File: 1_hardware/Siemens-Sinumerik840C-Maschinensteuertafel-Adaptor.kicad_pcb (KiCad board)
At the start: 2 copper layers, 235 x 118.7 mm, 81 parts, among them J1 ProgHeader, J111 SSW-132-24-L-D, J121 SSW-132-24-L-D, J2 Power, J3 Buttons, J4 Reserve2, SW1 TS-1187A-B-A-B, SW2 TS-1187A-B-A-B, U1 STM32F103C8T6, U10 PCA9555PW,118, U11 PCA9555PW,118, U2 AP22652AW6-7, U3 LD1117S33CTR, U4 PCA9555PW,118, U5 PCA9555PW,118, U6 PCA9555PW,118, U7 PCA9555PW,118, U8 PCA9555PW,118, U9 PCA9555PW,118, X1 16MHz

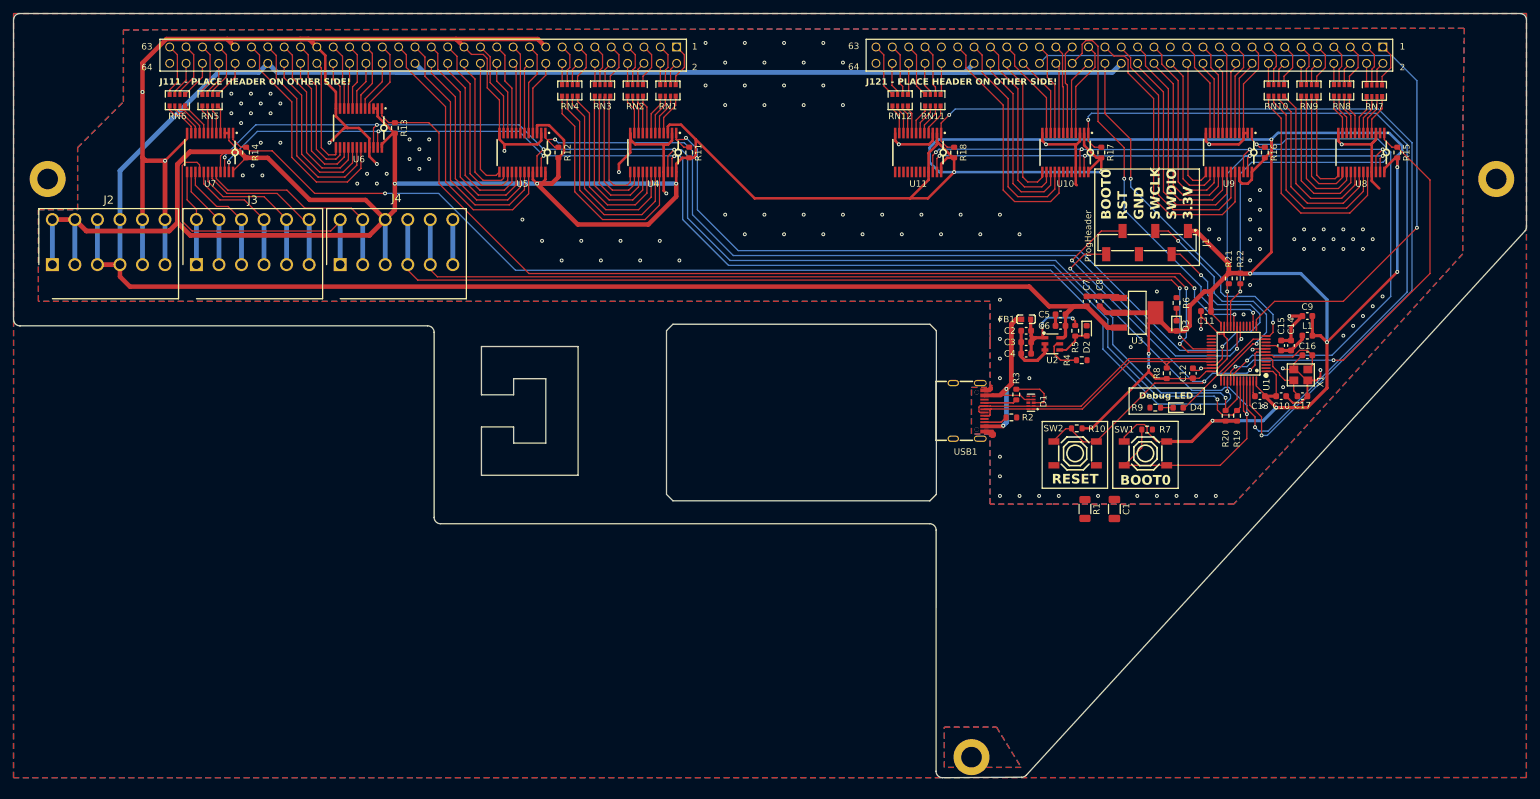
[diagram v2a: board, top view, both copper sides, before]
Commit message: changed from STM32F103C8 over to STM32L151C8 changed controller pinout, minor tweaks in board design, added labels and debug pads
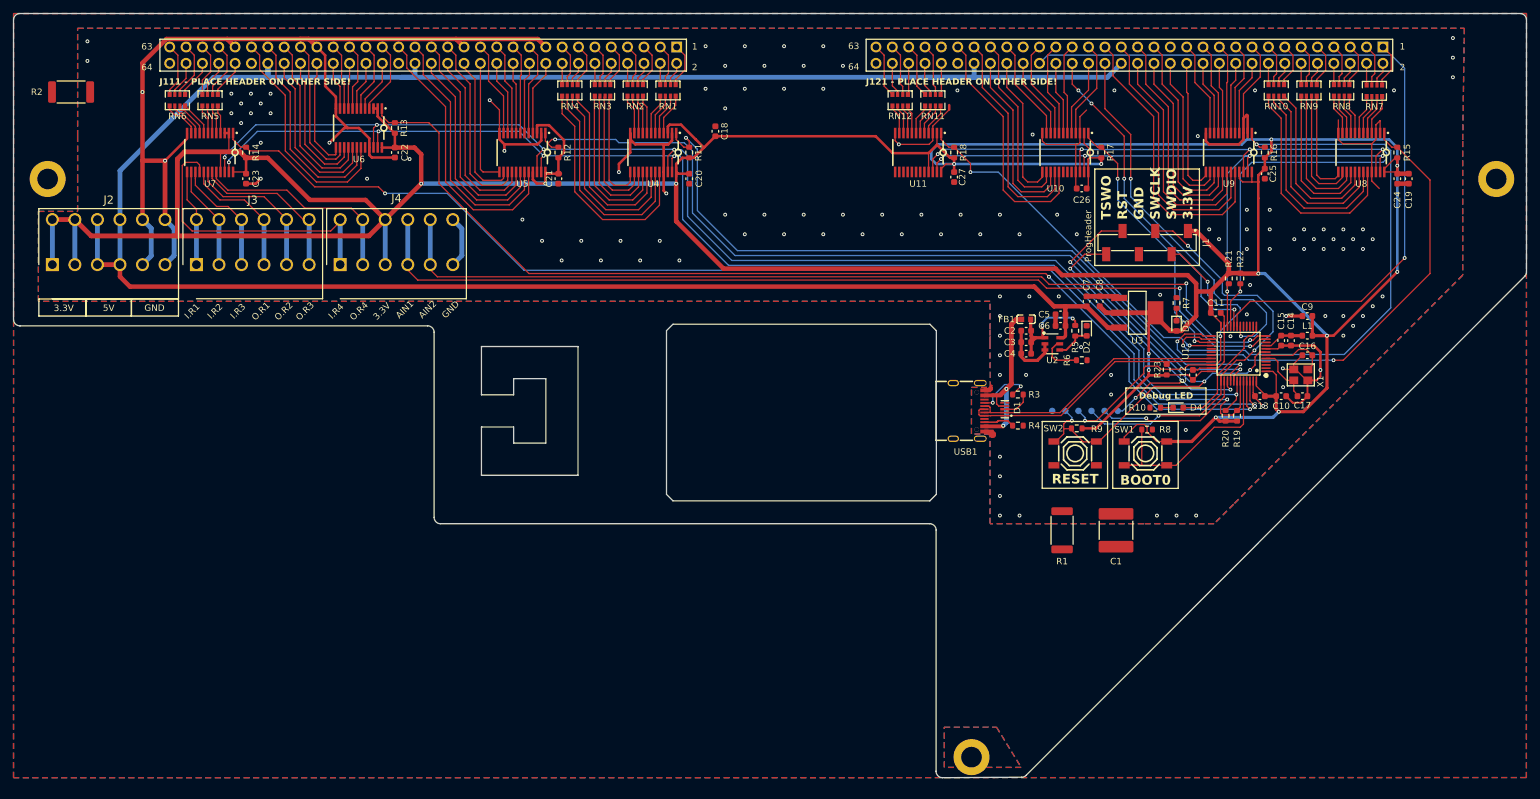
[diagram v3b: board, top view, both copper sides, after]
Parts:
- removed the R8 at (216.7, 81.4)
- added C18: 4u7, Capacitor_SMD:C_0603_1608Metric, F.Cu at (146.6, 43.8)
- added C19: 4u7, Capacitor_SMD:C_0603_1608Metric, F.Cu at (254.3, 51.1)
- added C20: 100n, Capacitor_SMD:C_0603_1608Metric, F.Cu at (142.5, 51.1)
- added C21: 100n, Capacitor_SMD:C_0603_1608Metric, F.Cu at (122.2, 51.1)
- added C22: 100n, Capacitor_SMD:C_0603_1608Metric, F.Cu at (96.8, 47.1)
- added C23: 100n, Capacitor_SMD:C_0603_1608Metric, F.Cu at (73.7, 51.1)
- added C24: 100n, Capacitor_SMD:C_0603_1608Metric, F.Cu at (252.5, 51.1)
- added C25: 100n, Capacitor_SMD:C_0603_1608Metric, F.Cu at (232.0, 50.4)
- added C26: 100n, Capacitor_SMD:C_0603_1608Metric, F.Cu at (203.5, 52.7)
- added C27: 100n, Capacitor_SMD:C_0603_1608Metric, F.Cu at (183.7, 50.9)
- added R2: 100k, Resistor_SMD:R_2512_6332Metric, F.Cu at (46.5, 37.7)
- added R23: 1k5, Resistor_SMD:R_0603_1608Metric, F.Cu at (216.7, 80.8)
- added TP1: JTDO-TraceSWO, TestPoint:TestPoint_Pad_D1.0mm, B.Cu at (209.1, 87.2)
- added TP2: JTDI, TestPoint:TestPoint_Pad_D1.0mm, B.Cu at (207.1, 87.2)
- added TP3: JTCK-SWCLK, TestPoint:TestPoint_Pad_D1.0mm, B.Cu at (205.0, 87.2)
- added TP4: JTMS-SWDIO, TestPoint:TestPoint_Pad_D1.0mm, B.Cu at (203.0, 87.2)
- added TP5: RESET, TestPoint:TestPoint_Pad_D1.0mm, B.Cu at (201.0, 87.2)
- added TP6: GND, TestPoint:TestPoint_Pad_D1.0mm, B.Cu at (198.9, 87.2)
- C1: footprint Capacitor_SMD:C_1206_3216Metric -> Capacitor_SMD:C_2220_5750Metric
- R1: footprint Resistor_SMD:R_1206_3216Metric -> Resistor_SMD:R_2512_6332Metric
- R10: renamed from R9; value 1k5 -> 470
- R5: value 10k -> 680
- R7: renamed from R6; value 1k5 -> 470
- RN1, RN10, RN11, RN12, RN2, RN3, RN4, RN5, RN6, RN7, RN8, RN9: value 4x680R -> 4x470R
- U1: value STM32F103C8T6 -> STM32L151C8T6
- moved R1 4.85 mm to (200.5, 105.8)
- moved D1 4.19 mm to (191.6, 87.0)
- moved C1 3.31 mm to (208.8, 105.8)
- moved R4 1.63 mm to (193.6, 89.5)
- moved C11 1.55 mm to (224.3, 72.0), turned to 180 degrees
- moved C14 0.76 mm to (236.0, 76.3), turned to 90 degrees
- moved C15 0.76 mm to (234.5, 76.3), turned to 90 degrees
- moved R3 0.25 mm to (193.6, 84.7), turned to 180 degrees
- moved C12 0.25 mm to (220.8, 81.6)
- renumbered R2 to R4, R4 to R6, R7 to R8, R10 to R9
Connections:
- J1 pad 6: BOOT0 -> TSWO
- U1 pad 11: DebugLED -> AIN1
- U1 pad 12: Button-~{A15} -> AIN2
- U1 pad 13: Button-~{D01} -> DebugLED
- U1 pad 14: Button-~{E01} -> unconnected-(U1-PA4-Pad14)
- U1 pad 18: EXP_INT1 -> Button-~{A15}
- U1 pad 19: EXP_INT2 -> Button-~{D01}
- U1 pad 20: EXP_INT3 -> Button-~{E01}
- U1 pad 25: unconnected-(U1-PB12-Pad25) -> EXP_INT5
- U1 pad 26: unconnected-(U1-PB13-Pad26) -> EXP_INT6
- U1 pad 27: unconnected-(U1-PB14-Pad27) -> EXP_INT7
- U1 pad 28: unconnected-(U1-PB15-Pad28) -> EXP_INT8
- U1 pad 29: AIN1 -> unconnected-(U1-PA8-Pad29)
- U1 pad 30: AIN2 -> unconnected-(U1-PA9-Pad30)
- U1 pad 38: unconnected-(U1-PA15-Pad38) -> /JTDI
- U1 pad 39: EXP_INT4 -> TSWO
- U1 pad 40: EXP_INT5 -> EXP_INT1
- U1 pad 41: EXP_INT6 -> EXP_INT2
- U1 pad 45: EXP_INT7 -> EXP_INT3
- U1 pad 46: EXP_INT8 -> EXP_INT4
- U10 pad 7: ENC1-X15 -> Button-E02
- U10 pad 8: Button-E02 -> ENC1-X15
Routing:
- net EXP_INT8: track 146.3 -> 57.2 mm
- net EXP_INT7: track 121.5 -> 42.2 mm
- net TSWO: track 0.00 -> 52.7 mm, vias 0 -> 4
- net +3V3: track 695.4 -> 741.1 mm
- net BOOT0: track 81.1 -> 36.2 mm, vias 2 -> 0
- net SWCLK: track 37.7 -> 64.5 mm, vias 2 -> 3
- net /JTDI: track 0.00 -> 23.2 mm, vias 0 -> 1
- net SWDIO: track 31.5 -> 52.5 mm, vias 2 -> 3
- net GND: track 373.0 -> 388.8 mm, vias 136 -> 129
- net EXP_INT5: track 64.0 -> 77.9 mm
- net EXP_INT3: track 153.7 -> 166.3 mm
- net EXP_INT6: track 78.5 -> 90.5 mm
- net Button-~{E01}: track 63.4 -> 53.2 mm, vias 2 -> 4
- net AIN1: track 142.2 -> 148.6 mm
- net AIN2: track 140.9 -> 145.8 mm
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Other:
- outline, holes or cut-outs redrawn
- board text added: "5V"
- board text added: "AIN1"
- board text added: "AIN2"
- board text added: "I.R1"
- board text added: "I.R2"
- board text added: "I.R3"
- board text added: "I.R4"
- board text added: "JTDI"
- board text added: "O.R1"
- board text added: "O.R2"
- board text added: "O.R3"
- board text added: "O.R4"
- board text added: "TSWO"
- board text added: "TraceSWO"

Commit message: finished v0.9.2
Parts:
- added G***: LOGO, LOGO, F.Cu at (168.5, 40.2)
- added R24: 0, Resistor_SMD:R_0603_1608Metric, F.Cu at (181.7, 55.7)
- added R25: 0, Resistor_SMD:R_0603_1608Metric, F.Cu at (179.9, 55.7)
- added R26: 0, Resistor_SMD:R_0603_1608Metric, F.Cu at (227.9, 65.4)
- added R27: 0, Resistor_SMD:R_0603_1608Metric, F.Cu at (226.1, 65.4)
- C12: renamed from C15; value 100n -> 1u
- C13: renamed from C14; value 1u -> 100n
- C19: value 4u7 -> 100n
- C23: value 100n -> 4u7
- RN1, RN10, RN11, RN12, RN2, RN3, RN4, RN5, RN6, RN7, RN8, RN9: value 4x470R -> 4x680R
- TP1: value JTDO-TraceSWO -> GND
- TP3: value JTCK-SWCLK -> JTMS-SWDIO
- TP4: value JTMS-SWDIO -> JTCK-SWCLK
- TP5: value RESET -> JTDO-TraceSWO
- TP6: value GND -> RESET
- moved R12 22.6 mm to (207.3, 78.1)
- moved R13 19.5 mm to (209.1, 78.1)
- moved R22 5.34 mm to (226.1, 61.3)
- moved R23 5.34 mm to (227.9, 61.3)
- moved C18 2.65 mm to (145.8, 41.2), turned to 180 degrees
- moved R8 0.06 mm to (216.7, 80.9)
- renumbered C12 to C14, C13 to C15, R9 to R11, R19 to R12, R20 to R13, R11 to R14, R12 to R15, R13 to R16, R14 to R17, R15 to R18, R16 to R19, R17 to R20, R18 to R21, R21 to R22, R22 to R23, R23 to R8, R8 to R9
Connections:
- net /JTDI renamed /Microcontroller/JTDI
- C18 pad 2: +3V3 -> VCC
- C19 pad 2: +3V3 -> VCC
- C20 pad 2: +3V3 -> VCC
- C21 pad 2: +3V3 -> VCC
- C22 pad 2: +3V3 -> VCC
- C23 pad 2: +3V3 -> VCC
- C24 pad 2: +3V3 -> VCC
- C25 pad 2: +3V3 -> VCC
- C26 pad 2: +3V3 -> VCC
- C27 pad 2: +3V3 -> VCC
- R12 pad 2: +3V3 -> VCC
- R13 pad 2: +3V3 -> VCC
- R14 pad 2: +3V3 -> VCC
- R15 pad 2: +3V3 -> VCC
- R16 pad 2: +3V3 -> VCC
- R17 pad 2: +3V3 -> VCC
- R18 pad 2: +3V3 -> VCC
- R19 pad 2: +3V3 -> VCC
- R20 pad 2: +3V3 -> VCC
- R21 pad 2: +3V3 -> VCC
- R22 pad 2: +3V3 -> VCC
- R23 pad 2: +3V3 -> VCC
- TP1 pad 1: TSWO -> GND
- TP3 pad 1: SWCLK -> SWDIO
- TP4 pad 1: SWDIO -> SWCLK
- TP5 pad 1: RST -> TSWO
- TP6 pad 1: GND -> RST
- U1 pad 18: Button-~{A15} -> unconnected-(U1-PB0-Pad18)
- U1 pad 19: Button-~{D01} -> unconnected-(U1-PB1-Pad19)
- U1 pad 20: Button-~{E01} -> unconnected-(U1-PB2-Pad20)
- U1 pad 21: I2C2_SCL -> Net-(U1-PB10)
- U1 pad 22: I2C2_SDA -> Net-(U1-PB11)
- U10 pad 10: Button-D02 -> Button-E02
- U10 pad 11: ENC1-X14 -> ENC1-X13
- U10 pad 13: Schluessel2 -> Button-~{D01}
- U10 pad 14: Button-A14 -> Button-D02
- U10 pad 15: Schluessel0 -> ENC1-X14
- U10 pad 16: Schluessel3 -> Schluessel2
- U10 pad 17: Button-A13 -> Button-A14
- U10 pad 18: unconnected-(U10-IO1_5-Pad18) -> Schluessel0
- U10 pad 19: unconnected-(U10-IO1_6-Pad19) -> Schluessel3
- U10 pad 2: +3V3 -> VCC
- U10 pad 20: unconnected-(U10-IO1_7-Pad20) -> Button-A13
- U10 pad 24: +3V3 -> VCC
- U10 pad 4: ENC1-X11 -> Button-~{A15}
- U10 pad 5: Button-A16 -> ENC1-X11
- U10 pad 6: ENC1-X12 -> Button-A16
- U10 pad 7: Button-E02 -> ENC1-X12
- U10 pad 8: ENC1-X15 -> Button-~{E01}
- U10 pad 9: ENC1-X13 -> ENC1-X15
- U11 pad 2: +3V3 -> VCC
- U11 pad 21: +3V3 -> VCC
- U11 pad 24: +3V3 -> VCC
- U4 pad 24: +3V3 -> VCC
- U4 pad 3: +3V3 -> VCC
- U5 pad 21: +3V3 -> VCC
- U5 pad 24: +3V3 -> VCC
- U5 pad 3: +3V3 -> VCC
- U6 pad 2: +3V3 -> VCC
- U6 pad 24: +3V3 -> VCC
- U6 pad 3: +3V3 -> VCC
- U7 pad 2: +3V3 -> VCC
- U7 pad 21: +3V3 -> VCC
- U7 pad 24: +3V3 -> VCC
- U7 pad 3: +3V3 -> VCC
- U8 pad 24: +3V3 -> VCC
- U9 pad 21: +3V3 -> VCC
- U9 pad 24: +3V3 -> VCC
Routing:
- net +3V3: track 741.1 -> 361.6 mm, vias 14 -> 5
- net VCC: track 372.8 -> 675.2 mm, vias 0 -> 5
- net Button-~{D01}: track 119.1 -> 23.3 mm, vias 1 -> 0
- net GND: track 388.8 -> 302.6 mm, vias 129 -> 113
- net Button-~{A15}: track 60.2 -> 12.7 mm, vias 2 -> 0
- net Button-~{E01}: track 53.2 -> 11.7 mm, vias 4 -> 0
- net ENC1-X14: track 15.9 -> 30.2 mm
- net Button-D02: track 12.6 -> 25.0 mm
- net Net-(U1-PB10): track 0.00 -> 8.40 mm
- net TSWO: track 52.7 -> 60.8 mm
- net Net-(U1-PB11): track 0.00 -> 7.89 mm
- net Schluessel2: track 23.2 -> 29.4 mm
- net Button-A14: track 29.2 -> 35.1 mm
- net Schluessel0: track 29.0 -> 34.7 mm
- net Schluessel3: track 35.0 -> 40.3 mm
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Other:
- board text added: "${ISSUE_DATE} ©PedPEx ${REVISION}"

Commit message: pcb v0.9.3 finished
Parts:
- removed the C5 at (200.2, 72.2)
- added C6: 100u, Capacitor_SMD:CP_Elec_5x5.8, F.Cu at (199.4, 69.9)
- C5: renamed from C6; value 120u -> 0.1u
- moved C7 0.51 mm to (204.8, 70.2)
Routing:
- net GND: track 302.6 -> 330.3 mm, vias 113 -> 116
- net +3V3: track 361.6 -> 363.9 mm
- net VCC: track 675.2 -> 676.2 mm

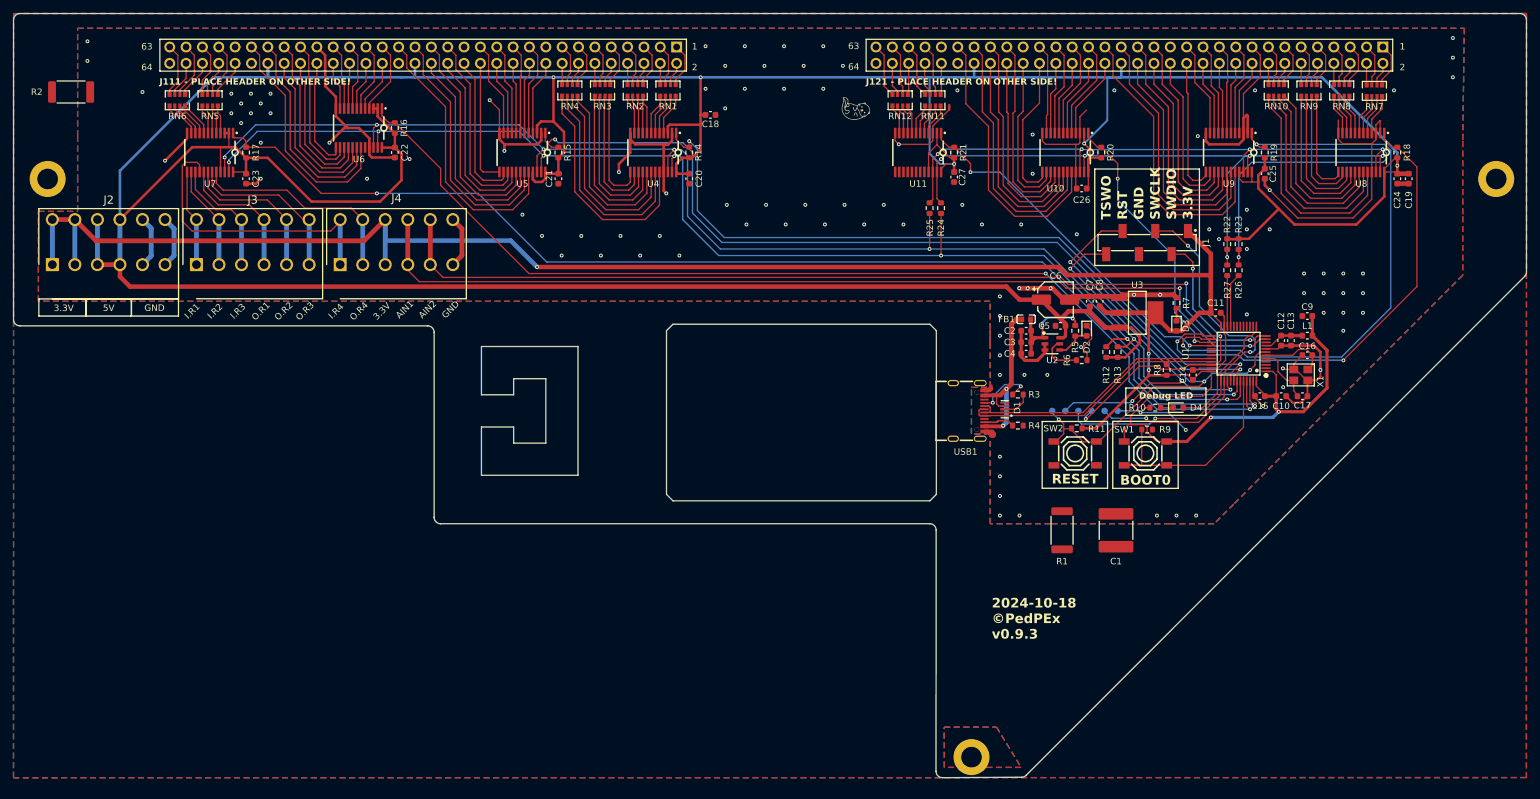
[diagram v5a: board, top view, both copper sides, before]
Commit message: PCB v0.9.4 - finished final prototype STM32 project reinitialised (F103C8 -> L151C8)
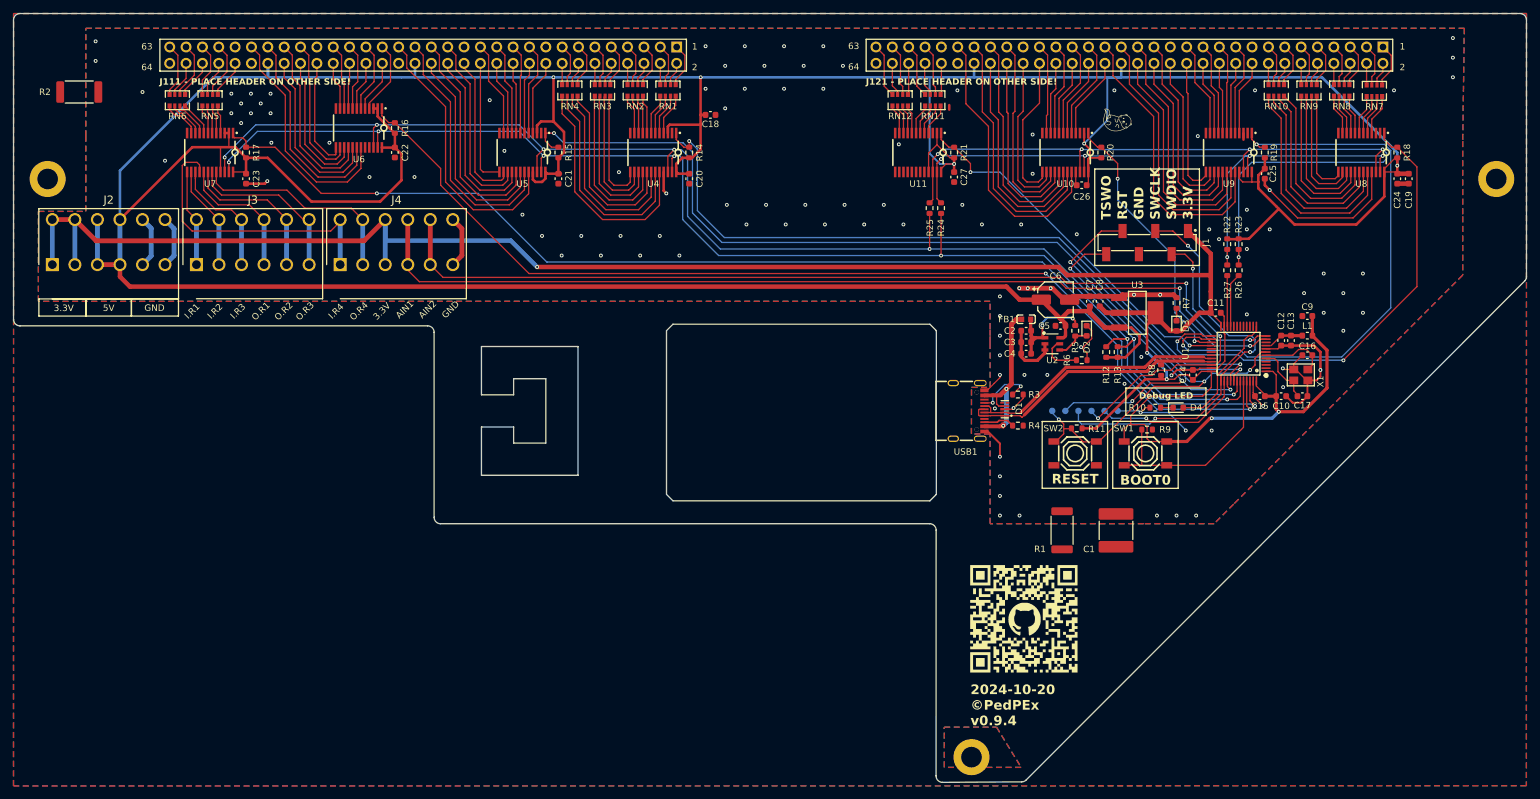
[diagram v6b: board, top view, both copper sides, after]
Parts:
- added G***: LOGO, project_library:QR_CODE, F.Cu at (194.5, 119.5)
- D1: footprint easyeda2kicad:USON-10_L2.5-W1.0-P0.50-BL -> project_library:USON-10_L2.5-W1.0-P0.50-BL
- G***: footprint LOGO -> project_library:LOGO
- H1, H2, H3: footprint MountingHole:MountingHole_3.2mm_M3_DIN965_Pad -> project_library:MountingHole_3.2mm_M3_DIN965_Pad
- J1: footprint easyeda2kicad:HDR-SMD_6P-P2.54-V-M-LS4.8_R2 -> project_library:HDR-SMD_6P-P2.54-V-M-LS4.8_R2
- J111, J121: footprint CostumLibrary:SAMTEC_SSW-132-24-L-D -> project_library:SAMTEC_SSW-132-24-L-D
- J2, J3, J4: footprint CostumLibrary:1824460000 - LSF-SMT 3.500690 3.5SN BK TU -> project_library:1824460000 - LSF-SMT 3.500690 3.5SN BK TU
- RN1, RN10, RN11, RN12, RN2, RN3, RN4, RN5, RN6, RN7, RN8, RN9: footprint easyeda2kicad:RES-ARRAY-SMD_0603-8P-L3.2-W1.6-BL -> project_library:RES-ARRAY-SMD_0603-8P-L3.2-W1.6-BL
- SW1, SW2: footprint easyeda2kicad:SW-SMD_4P-L5.1-W5.1-P3.70-LS6.5-TL-2 -> project_library:SW-SMD_4P-L5.1-W5.1-P3.70-LS6.5-TL-2
- U1: footprint easyeda2kicad:LQFP-48_L7.0-W7.0-P0.50-LS9.0-BL -> project_library:LQFP-48_L7.0-W7.0-P0.50-LS9.0-BL
- U10, U11, U4, U5, U6, U7, U8, U9: footprint easyeda2kicad:TSSOP-24_L7.8-W4.4-P0.65-LS6.4-BL -> project_library:TSSOP-24_L7.8-W4.4-P0.65-LS6.4-BL
- U2: footprint easyeda2kicad:SOT-23-6_L2.9-W1.6-P0.95-LS2.8-BL -> project_library:SOT-23-6_L2.9-W1.6-P0.95-LS2.8-BL
- U3: footprint easyeda2kicad:SOT-223-4_L6.5-W3.5-P2.30-LS7.0-BR -> project_library:SOT-223-4_L6.5-W3.5-P2.30-LS7.0-BR
- USB1: footprint easyeda2kicad:USB-C-SMD_KH-TYPE-C-16P -> project_library:USB-C-SMD_KH-TYPE-C-16P
- X1: footprint easyeda2kicad:CRYSTAL-SMD_4P-L3.2-W2.5-BL_SIT8008BI -> project_library:CRYSTAL-SMD_4P-L3.2-W2.5-BL_SIT8008BI
- moved G*** 40.7 mm to (209.1, 42.0)
- moved R2 1.27 mm to (47.8, 37.7)
- moved R8 0.86 mm to (215.8, 80.9)
- moved C26 0.51 mm to (203.5, 52.2)
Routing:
- net GND: track 330.3 -> 182.3 mm, vias 116 -> 117
- net +3V3: track 363.9 -> 367.0 mm
- net USB_VBUS: track 32.9 -> 35.5 mm
- net SWDIO: track 47.6 -> 45.1 mm
- net +3V3A: track 6.28 -> 5.48 mm
- net USB_D+: track 41.8 -> 42.3 mm
- net EXP_INT2: track 134.0 -> 134.6 mm
- net VCC: track 676.2 -> 675.7 mm
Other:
- board size 235 x 118.7 mm -> 235 x 119.4 mm

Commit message: PCB v0.9.5 - finished final prototype STM32 project pinout corrected
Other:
- board text added: "JLCJLCJLCJLCJLC"
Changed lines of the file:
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@@
 	(title_block
 		(title "Siemens-LinuxCNC-Interface")
-		(date "2024-10-20")
-		(rev "v0.9.4")
+		(date "2024-10-27")
+		(rev "v0.9.5")
 	)
 	(layers
@@
 		(tags "capacitor")
 		(property "Reference" "C1"
-			(at 2.921 4.191 360)
+			(at 2.921 4.191 0)
 			(layer "F.SilkS")
 			(effects
@@
 	)
 	(gr_rect
+		(start 153.927 41.361)
+		(end 163.927 51.361)
+		(stroke
+			(width 0.2)
+			(type solid)
+		)
+		(fill solid)
+		(layer "F.SilkS")
+	)
+	(gr_rect
 		(start 170.026768 29.483907)
 		(end 251.810922 34.433759)
@@
 		)
 	)
+	(gr_text "JLCJLCJLCJLCJLC"
+		(at 206.552 61.681 0)
+		(layer "F.SilkS")
+		(effects
+			(font
+				(size 1 1)
+				(thickness 0.15)
+			)
+			(justify left bottom)
+		)
+	)
 	(gr_text "O.R1"
 		(at 75.996 71.714 45)
@@
 			(thermal_gap 0.3)
 			(thermal_bridge_width 0.5)
-			(smoothing chamfer)
-			(radius 1)
 			(hatch_thickness 2)
 			(hatch_gap 1.5)

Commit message: started with PCB v0.9.6, software WIP communication with expander working, able to read inputs and set outputs, matrix for properly key-mapping and serial still needs to be done bugs from first badge of boards need to be fixed for version v1.0 -> (upcoming) changelog for v0.9.6  - PullUp Resistor on USB+ not needed  - for DFU to be working, BOOT1 (PB2) needs to be tied to GND  - second I2C bus not needed -> will be combined into one  - ...
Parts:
- U1: value STM32L151C8T6 -> STM32L151CCT6
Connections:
- U1 pad 20: unconnected-(U1-PB2-Pad20) -> GND
